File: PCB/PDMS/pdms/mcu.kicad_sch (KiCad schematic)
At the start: 26 parts, among them J2 DBG, U1 STM32F405RGTx, Y1 16Mhz, Y2 32KHz

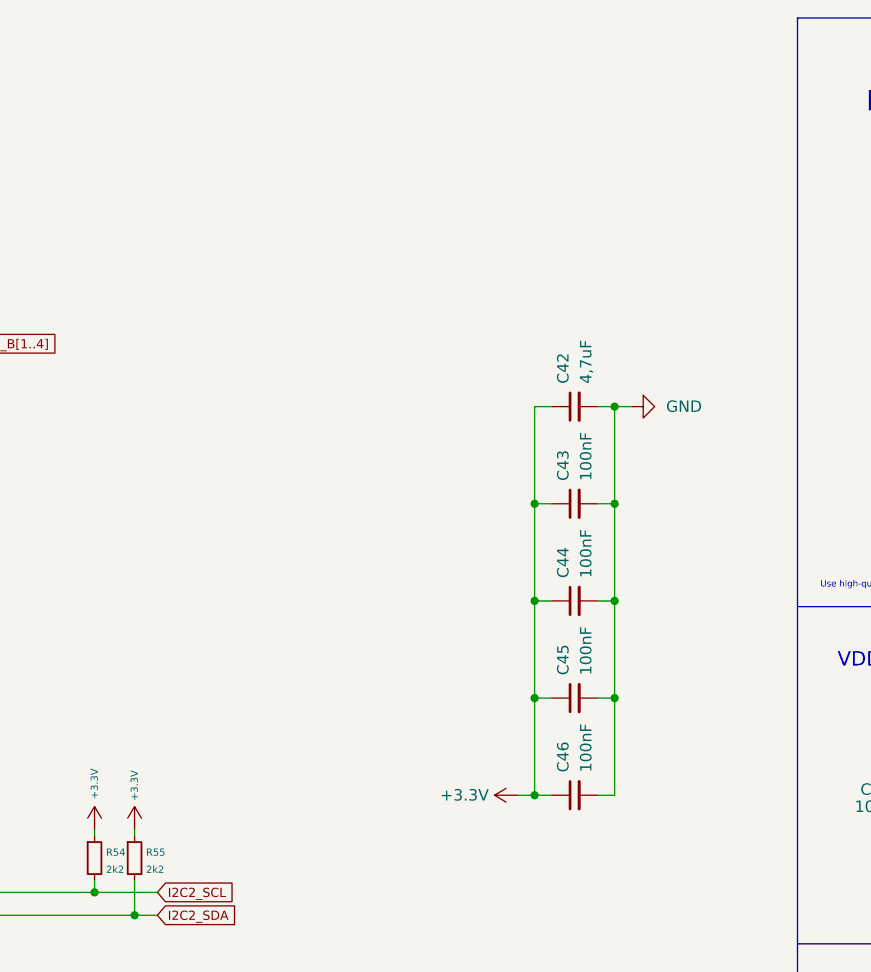
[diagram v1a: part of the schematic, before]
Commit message: Schematic refactoring
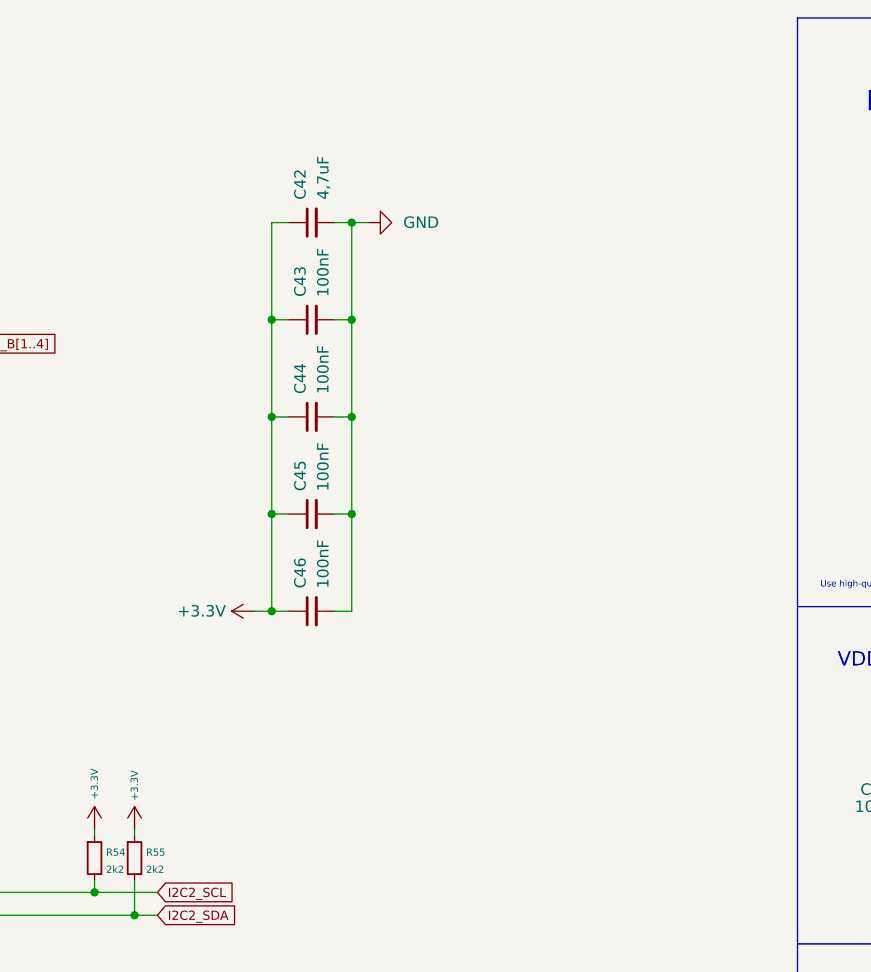
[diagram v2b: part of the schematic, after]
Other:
- moved on the sheet: C42, C43, C44, C45, C46
